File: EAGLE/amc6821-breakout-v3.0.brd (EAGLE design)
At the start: 45.7 x 45.8 mm, 68 parts, among them J1 QWIIC_RIGHT_ANGLE, J10 455-1750-1-ND, J2 QWIIC_RIGHT_ANGLE, J5 KK-254-4KK-254, J6 FAN No2, Q1 2N3904, Q2 2N7002, Q5 NDT3055L, U1 AMC6821-Q1QSOP-16N, U2 SN74LVC2G14DCKR, U3 SN74LVC2G14DCKR, U4 LD1117-33, U5 7805TV

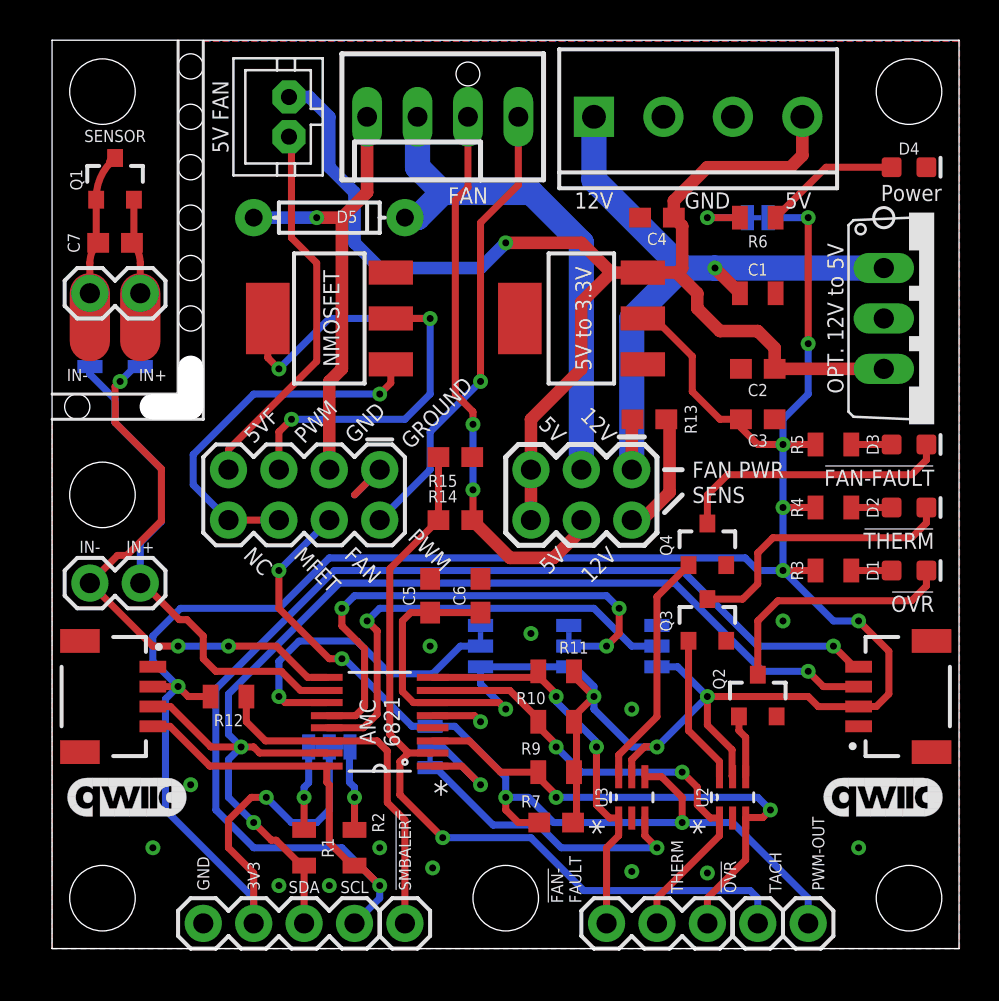
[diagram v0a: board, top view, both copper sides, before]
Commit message: v3 upload - split into 2 boards
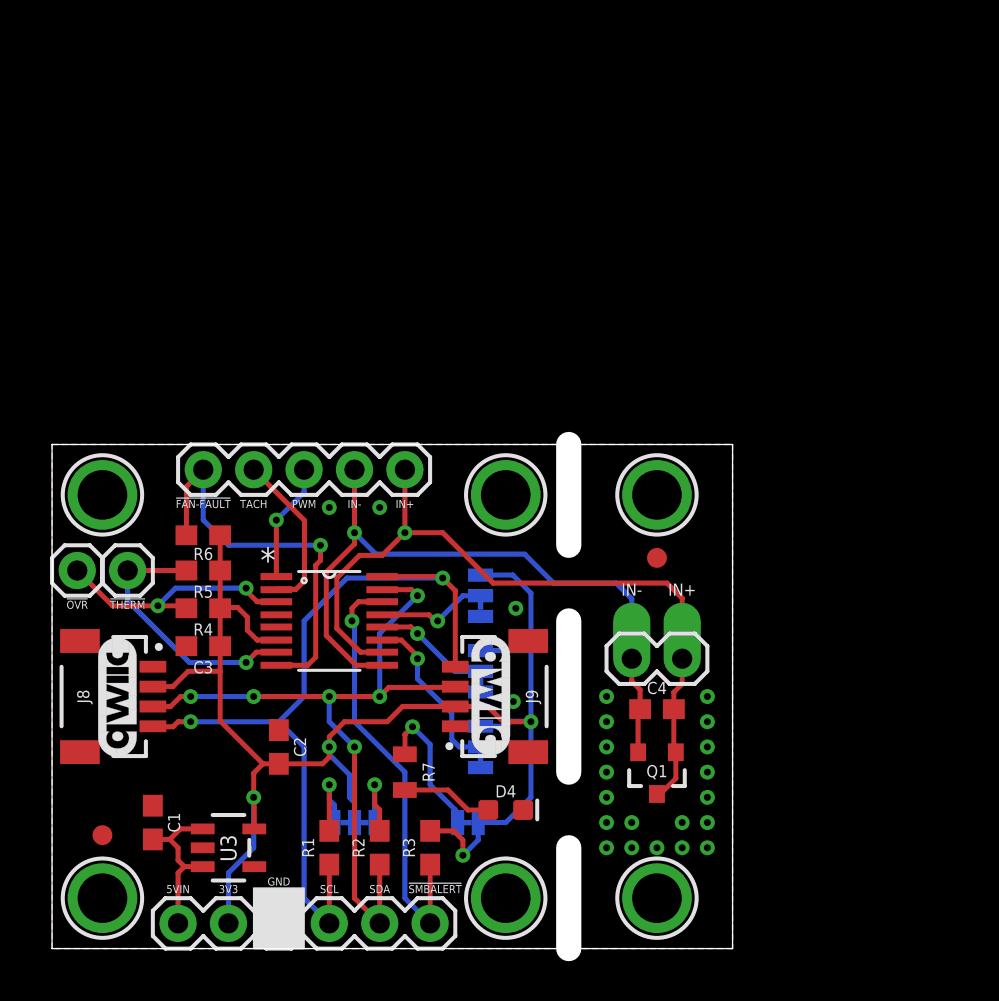
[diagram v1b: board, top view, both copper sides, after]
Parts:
- removed C5: 10uF, SparkFun-Capacitors:0603
- removed C6: 0.1uF, SparkFun-Capacitors:0603
- removed C7: 1nF, SparkFun-Capacitors:0603
- removed D1, D2, D3: RED, SparkFun-LED:LED-0603
- removed D5: 200mA/100V/1V, SparkFun-DiscreteSemi:DIODE-1N4148
- removed H1, H2, H3, H4, H5, H6: STAND-OFF, SparkFun-Hardware:STAND-OFF
- removed J1, J2: QWIIC_RIGHT_ANGLE, SparkFun-Connectors:JST04_1MM_RA
- removed J10: 455-1750-1-ND, SparkFun-Connectors:1X03
- removed J11, J12, J13: (no value), SparkFun-Connectors:1X01
- removed J14: (no value), SparkFun-Connectors:1X02
- removed JP4: JUMPER-SMT_3_1-NC_TRACE_SILK, SparkFun-Jumpers:SMT-JUMPER_3_1-NC_TRACE_SILK
- removed JP6, JP7: JUMPER-SMT_2_NC_TRACE_SILK, SparkFun-Jumpers:SMT-JUMPER_2_NC_TRACE_SILK
- removed JP8: (no value), SparkFun-Connectors:2X4
- removed JP9: (no value), SparkFun-Connectors:2X3-NS
- removed Q2: 2N7002, VinoRodrigues_Custom_Eagle:SOT23-3
- removed Q3, Q4: (no value), VinoRodrigues_Custom_Eagle:SOT23-3
- removed Q5: NDT3055L, VinoRodrigues_Custom_Eagle:SOT223
- removed R10, R11, R12, R9: 4.7K, SparkFun-Resistors:0805
- removed R13, R14: 10k, SparkFun-Resistors:0603
- removed R15: 4.7k, SparkFun-Resistors:0603
- removed U2: SN74LVC2G14DCKR, VinoRodrigues_Custom_Eagle:SOT65P210X110-6N
- removed U4: LD1117-33, SparkFun-IC-Power:SOT223
- removed U5: 7805TV, linear:TO220V
- added FID3, FID4: FIDUCIAL_1MM, microbuilder:FIDUCIAL_1MM
- added J7: (no value), VinoRodrigues_Custom_Eagle:1X02-LONG
- added J8: QWIIC_RIGHT_ANGLE, VinoRodrigues_Custom_Eagle:JST04_1MM_RA
- added U$10, U$4, U$5, U$7, U$8, U$9: MOUNTINGHOLE2.5, microbuilder:MOUNTINGHOLE_2.5_PLATED
- C1: value 0.33µF -> 10uF; device SparkFun-Capacitors:0805 -> SparkFun-Capacitors:0603
- C2: value 0.1uF -> 10uF
- C3: value 10uF -> 0.1uF
- C4: value 10uF -> 1nF
- J3: device SparkFun-Connectors:1X04 -> SparkFun-Connectors:1X05
- J4: device SparkFun-Connectors:SCREWTERMINAL-3.5MM-4 -> SparkFun-Connectors:1X06
- J5: value KK-254-4KK-254 -> (none); device VinoRodrigues_Custom_Eagle:MOLEX_47053-1000 -> SparkFun-Connectors:1X01
- J6: value FAN No2 -> (none); device VinoRodrigues_Custom_Eagle:JST-PH2 -> SparkFun-Connectors:1X01
- J9: value (none) -> QWIIC_RIGHT_ANGLE; device SparkFun-Connectors:1X02 -> VinoRodrigues_Custom_Eagle:JST04_1MM_RA
- R1, R2: value 4.7K -> 2.2k; device SparkFun-Resistors:0805 -> SparkFun-Resistors:0603
- R3, R4, R5, R6: value 1K -> 2.2k; device SparkFun-Resistors:0805 -> SparkFun-Resistors:0603
- R7: value 2.2k -> 1K; device SparkFun-Resistors:0603 -> SparkFun-Resistors:0805
- U3: value SN74LVC2G14DCKR -> AP2112K-3.3; device VinoRodrigues_Custom_Eagle:SOT65P210X110-6N -> microbuilder:SOT23-5
- moved J4 45.7 mm to (6.35, 1.27)
- moved C1 40.5 mm to (5.08, 6.35), turned to 90 degrees
- moved Q1 40.5 mm to (30.5, 8.89), turned to 180 degrees
- moved D4 38.2 mm to (22.9, 6.99)
- moved JP5 33.8 mm to (21.0, 6.35)
- moved R5 32.4 mm to (7.62, 19.1)
- moved R6 32.2 mm to (7.62, 20.8), turned to 0 degrees
- moved R4 32.2 mm to (7.62, 17.1), turned to 0 degrees
- moved LOGO1 31.3 mm to (12.7, 17.9), turned to 0 degrees
- moved C2 30.7 mm to (11.4, 10.2), turned to 90 degrees
- moved C3 30.2 mm to (7.62, 15.2), turned to 180 degrees
- moved J5 29.4 mm to (1.27, 19.1), turned to 0 degrees
- moved J9 27.4 mm to (20.3, 12.7), turned to 90 degrees
- moved U$1 27.3 mm to (8.26, 9.53), turned to 0 degrees
- moved J3 25.0 mm to (17.8, 24.1), turned to 180 degrees
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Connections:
- removed net !PWM-OUT: JP4.3, U3.3
- removed net 12V: C1.1, J4.1, JP9.1, R13.1, U5.1
- removed net FAN-FAULT: Q4.1, U3.6
- removed net FAN-GND: D5.A, J5.1:GND, JP8.3
- removed net GND-5V: J6.2, JP8.7
- removed net GND-PWM: JP8.5, Q5.D, Q5.D2
- removed net N$10: D3.C, Q4.3
- removed net N$11: D1.A, R3.1
- removed net N$14: D1.C, Q2.3
- removed net N$15: D2.C, Q3.3
- removed net N$16: D2.A, R4.1
- removed net N$17: J5.3:TACH, JP9.4, R14.2
- removed net N$18: JP9.2, R13.2
- removed net N$2: C7.2, J9.1, JP6.2, Q1.1, Q1.3
- removed net N$7: C7.1, J9.2, JP7.2, Q1.2
- removed net N$9: D3.A, R5.2
- removed net OVR: Q2.1, U2.4
- removed net PWM-FAN: J5.4:PWM, JP8.2
- removed net PWM-MF: JP8.6, JP8.8, Q5.G
- removed net PWM-OUT: J12.1, JP4.1, JP8.4, R7.1, U3.4
- removed net THERM: Q3.1, U2.6
- removed net VDD: D5.C, J5.2:+12VDC, JP9.3
- net !FAN-FAULT: now also J3.5, R6.1; no longer J10.1, R11.1, U3.1
- net !OVR: now also J5.1, R4.1; no longer J10.3, R9.1, U2.3
- net !SMBALERT: now also J4.6, R3.1; no longer J11.1, R12.1
- net !THERM: now also J6.1, R5.1; no longer J10.2, R10.1, U2.1
- net 3V3: now also C2.1, J4.2, J8.2, J9.2, R5.2, R6.2; no longer C5.1, C6.1, J1.2, J2.2, J3.2, R10.2, R11.2, R12.2, R5.1, R7.2, R9.2, U2.5, U4.2
- net 5V: now also C1.1, J4.1, U3.1, U3.3; no longer C2.1, C4.1, J4.4, J6.1, JP9.5, JP9.6, U4.3, U5.3
- net GND: now also J8.1, J8.NC1, J8.NC2, J9.1, J9.NC1, J9.NC2; no longer C4.2, C5.2, C6.2, J1.1, J2.1, J3.1, J4.2, JP8.1, Q2.2, Q3.2, Q4.2, Q5.S, R15.1, U2.2, U4.1, U5.2
- net IN+: now also C4.2, J3.1, J7.2, Q1.1, Q1.3; no longer J14.1, JP6.1
- net IN-: now also C4.1, J3.2, J7.1, Q1.2; no longer J14.2, JP7.1
- net N$12: now also R7.2; no longer R6.2
- net N$3: now also R2.1; no longer R1.1
- net N$4: now also R1.1; no longer R2.1
- net N$8: now also R7.1; no longer R6.1
- net PWM: now also J3.3; no longer JP4.2
- net SCL: now also J4.4, J8.4, J9.4, R1.2; no longer J1.4, J2.4, J3.4, R2.2
- net SDA: now also J4.5, J8.3, J9.3, R2.2; no longer J1.3, J2.3, J3.3, R1.2
- net TACH: now also J3.4; no longer J13.1, R14.1, R15.2
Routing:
- net 3V3: track 173.7 -> 77.4 mm, vias 12 -> 4
- net 5V: track 68.2 -> 8.32 mm, vias 1 -> 0
- net PWM-OUT: track 46.3 -> 0.00 mm, vias 4 -> 0
- net 12V: track 35.2 -> 0.00 mm, vias 1 -> 0
- net TACH: track 41.3 -> 8.26 mm, vias 1 -> 0
- net SCL: track 72.2 -> 41.9 mm
- net N$17: track 28.3 -> 0.00 mm, vias 2 -> 0
- net GND-PWM: track 27.5 -> 0.00 mm, vias 3 -> 0
- net VDD: track 26.2 -> 0.00 mm
- net PWM-FAN: track 23.2 -> 0.00 mm, vias 1 -> 0
- net FAN-GND: track 23.0 -> 0.00 mm, vias 1 -> 0
- net SDA: track 59.8 -> 38.9 mm, vias 3 -> 6
- net N$6: track 26.1 -> 5.89 mm, vias 3 -> 1
- net GND-5V: track 19.2 -> 0.00 mm
- net PWM-MF: track 19.0 -> 0.00 mm, vias 1 -> 0
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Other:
- board size 45.7 x 45.8 mm -> 34.3 x 25.4 mm
- board text added: "(c) 2012 Tecsmith by: Vino Rodrigues"
- board text added: "5VIN"
- board text added: "AMC6821 Breakout http://c1k.it/amc6 Qwiic / STEMMA QT"
- board text added: "AMC6821 Breakout http://c1k.it/amc6 Temperature Sensor"
- board text added: "Gnd"
- board text added: "Rev. 3.0"
- board text added: "Vdd"
- board text added: "Vdd A1 Gnd"
- board text added: "Vdd PWM-MODE Gnd"
- board text removed: "!FAN- FAULT"
- board text removed: "!FAULT"
- board text removed: "!SMBA"
- board text removed: "+"
- board text removed: "-"
- board text removed: "12V"
- board text removed: "3-Wire"
- board text removed: "4-Wire"
- board text removed: "5V"
- board text removed: "5V FAN"
- board text removed: "5V to 3.3V"
- board text removed: "5V-Fan"
- board text removed: "5VF"
- board text removed: "A1"
- board text removed: "AMC 6821"
- board text removed: "AMC6821 Breakout Board | Rel 2.3 (c) 2020 Vino Rodrigues"
- board text removed: "FAN"
- board text removed: "FAN PWR"
- board text removed: "FAN SENS"
- board text removed: "GND 3V3 SDA SCL"
- board text removed: "GROUND"
- board text removed: "MFET"
- board text removed: "NC"
- board text removed: "NMOSFET"
- board text removed: "OPT. 12V to 5V"
- board text removed: "Off"
- board text removed: "Opensource Hardware http://c1k.it/amc6"
- board text removed: "PWM-OUT"
- board text removed: "PWM/M"
- board text removed: "PWM\\!PWM"
- board text removed: "Power"
- board text removed: "SENS"
- board text removed: "SENSOR"
- board text removed: "TEMP. SENSOR"
- board text removed: "THERM"
- board text removed: "U2"
- board text removed: "U3"
- board text removed: "VDD"
- board text removed: "http://tecsmith.com.au"

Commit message: move C3 closer to the IC
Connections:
- net 3V3: now also C3.2; no longer C3.1
- net GND: now also C3.1; no longer C3.2
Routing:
- net 3V3: track 77.4 -> 74.2 mm
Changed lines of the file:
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@@
 <drawing>
 <settings>
-<setting alwaysvectorfont="yes"/>
+<setting alwaysvectorfont="no"/>
 <setting verticaltext="up"/>
 </settings>
@@
 <contactref element="J4" pad="2"/>
 <contactref element="U3" pad="5"/>
-<contactref element="C3" pad="1"/>
 <wire x1="10.1901" y1="6.03" x2="10.1901" y2="7.5899" width="0.254" layer="1"/>
 <wire x1="10.1901" y1="7.5899" x2="10.16" y2="7.62" width="0.254" layer="1"/>
@@
 <wire x1="8.47" y1="20.828" x2="8.47" y2="19.05" width="0.254" layer="1"/>
 <wire x1="8.47" y1="19.05" x2="8.47" y2="17.145" width="0.254" layer="1"/>
-<wire x1="8.47" y1="17.145" x2="8.47" y2="15.24" width="0.254" layer="1"/>
 <wire x1="9.8425" y1="16.03866875" x2="9.8425" y2="16.7005" width="0.254" layer="1"/>
 <wire x1="11.303" y1="15.5448" x2="10.33636875" y2="15.5448" width="0.254" layer="1"/>
@@
 <wire x1="8.47" y1="11.469" x2="8.47" y2="13.97" width="0.254" layer="1"/>
 <via x="24.13" y="11.43" extent="1-16" drill="0.35"/>
-<wire x1="8.47" y1="13.97" x2="8.47" y2="15.24" width="0.254" layer="1"/>
 <wire x1="24.13" y1="11.43" x2="24.13" y2="15.0114" width="0.254" layer="16"/>
 <wire x1="24.13" y1="15.0114" x2="24.13" y2="17.907" width="0.254" layer="16"/>
@@
 <wire x1="20.701" y1="5.461" x2="20.701" y2="4.699" width="0.254" layer="1"/>
 <wire x1="20.232" y1="5.93" x2="20.701" y2="5.461" width="0.254" layer="1"/>
+<contactref element="C3" pad="2"/>
+<wire x1="6.77" y1="15.24" x2="8.47" y2="17.145" width="0" layer="19" extent="1-1"/>
+<wire x1="5.08" y1="13.2" x2="6.77" y2="15.24" width="0" layer="19" extent="1-1"/>
 </signal>
 <signal name="GND">
@@
 <contactref element="J4" pad="3"/>
 <contactref element="U3" pad="2"/>
-<contactref element="C3" pad="2"/>
 <contactref element="J8" pad="NC2"/>
 <contactref element="J8" pad="NC1"/>
@@
 <via x="13.97" y="22.225" extent="1-16" drill="0.35"/>
 <via x="16.51" y="22.225" extent="1-16" drill="0.35"/>
+<contactref element="C3" pad="1"/>
+<wire x1="33.02" y1="11.43" x2="33.02" y2="12.7" width="0" layer="19" extent="1-1"/>
+<wire x1="33.02" y1="10.16" x2="33.02" y2="11.43" width="0" layer="19" extent="1-1"/>
+<wire x1="33.02" y1="8.89" x2="33.02" y2="10.16" width="0" layer="19" extent="1-1"/>
+<wire x1="33.02" y1="7.62" x2="33.02" y2="8.89" width="0" layer="19" extent="1-1"/>
+<wire x1="33.02" y1="6.35" x2="33.02" y2="7.62" width="0" layer="19" extent="1-1"/>
+<wire x1="33.02" y1="5.08" x2="33.02" y2="6.35" width="0" layer="19" extent="1-1"/>
+<wire x1="31.75" y1="5.08" x2="33.02" y2="5.08" width="0" layer="19" extent="1-1"/>
+<wire x1="30.48" y1="5.08" x2="31.75" y2="5.08" width="0" layer="19" extent="1-1"/>
+<wire x1="31.75" y1="6.35" x2="33.02" y2="6.35" width="0" layer="19" extent="1-1"/>
+<wire x1="29.21" y1="5.08" x2="30.48" y2="5.08" width="0" layer="19" extent="1-1"/>
+<wire x1="27.94" y1="5.08" x2="29.21" y2="5.08" width="0" layer="19" extent="1-1"/>
+<wire x1="27.94" y1="6.35" x2="27.94" y2="5.08" width="0" layer="19" extent="1-1"/>
+<wire x1="27.94" y1="7.62" x2="27.94" y2="6.35" width="0" layer="19" extent="1-1"/>
+<wire x1="27.94" y1="8.89" x2="27.94" y2="7.62" width="0" layer="19" extent="1-1"/>
+<wire x1="27.94" y1="10.16" x2="27.94" y2="8.89" width="0" layer="19" extent="1-1"/>
+<wire x1="27.94" y1="11.43" x2="27.94" y2="10.16" width="0" layer="19" extent="1-1"/>
+<wire x1="27.94" y1="12.7" x2="27.94" y2="11.43" width="0" layer="19" extent="1-1"/>
+<wire x1="29.21" y1="6.35" x2="29.21" y2="5.08" width="0" layer="19" extent="1-1"/>
+<wire x1="23.995" y1="9.9" x2="27.94" y2="10.16" width="0" layer="19" extent="1-1"/>
+<wire x1="21.59" y1="9.1186" x2="23.995" y2="9.9" width="0" layer="19" extent="1-16"/>
+<wire x1="20.32" y1="11.2" x2="21.59" y2="9.1186" width="0" layer="19" extent="1-16"/>
+<wire x1="21.59" y1="12.9286" x2="20.32" y2="11.2" width="0" layer="19" extent="1-16"/>
+<wire x1="23.241" y1="12.446" x2="21.59" y2="12.9286" width="0" layer="19" extent="16-16"/>
+<wire x1="23.737" y1="6.985" x2="23.995" y2="9.9" width="0" layer="19" extent="1-1"/>
+<wire x1="23.995" y1="15.5" x2="23.241" y2="12.446" width="0" layer="19" extent="1-1"/>
+<wire x1="23.368" y1="17.145" x2="23.995" y2="15.5" width="0" layer="19" extent="1-1"/>
+<wire x1="21.59" y1="16.7386" x2="23.368" y2="17.145" width="0" layer="19" extent="16-16"/>
+<wire x1="16.51" y1="22.225" x2="21.59" y2="16.7386" width="0" layer="19" extent="16-16"/>
+<wire x1="13.97" y1="22.225" x2="16.51" y2="22.225" width="0" layer="19" extent="1-1"/>
+<wire x1="11.303" y1="16.2052" x2="13.97" y2="22.225" width="0" layer="19" extent="1-1"/>
+<wire x1="8.47" y1="15.24" x2="11.303" y2="16.2052" width="0" layer="19" extent="1-1"/>
+<wire x1="5.08" y1="14.2" x2="8.47" y2="15.24" width="0" layer="19" extent="1-1"/>
+<wire x1="1.405" y1="15.5" x2="5.08" y2="14.2" width="0" layer="19" extent="1-1"/>
+<wire x1="11.43" y1="11.01" x2="8.47" y2="15.24" width="0" layer="19" extent="1-1"/>
+<wire x1="1.405" y1="9.9" x2="1.405" y2="15.5" width="0" layer="19" extent="1-1"/>
+<wire x1="5.08" y1="7.2" x2="1.405" y2="9.9" width="0" layer="19" extent="1-1"/>
+<wire x1="7.5899" y1="5.08" x2="5.08" y2="7.2" width="0" layer="19" extent="1-1"/>
+<wire x1="11.43" y1="1.27" x2="7.5899" y2="5.08" width="0" layer="19" extent="1-1"/>
 </signal>
 <signal name="N$3">

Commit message: minor rename, JP4
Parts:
- renumbered JP5 to JP4
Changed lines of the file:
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@@
 <attribute name="NAME" x="15.24" y="7.493" size="0.6096" layer="26" font="vector" ratio="20" rot="MR0" align="bottom-center"/>
 </element>
-<element name="JP5" library="SparkFun-Jumpers" package="SMT-JUMPER_2_NC_TRACE_SILK" package3d_urn="urn:adsk.eagle:package:39281/1" value="JUMPER-SMT_2_NC_TRACE_SILK" x="20.955" y="6.35" smashed="yes" rot="MR180"/>
+<element name="JP4" library="SparkFun-Jumpers" package="SMT-JUMPER_2_NC_TRACE_SILK" package3d_urn="urn:adsk.eagle:package:39281/1" value="JUMPER-SMT_2_NC_TRACE_SILK" x="20.955" y="6.35" smashed="yes" rot="MR180"/>
 <element name="LOGO1" library="SparkFun-Aesthetics" package="OSHW-LOGO-S" value="OSHW-LOGOS" x="12.7" y="17.907" smashed="yes" rot="MR0"/>
 <element name="LOGO2" library="SparkFun-Aesthetics" package="QWIIC_6MM" value="QWIIC_LOGO_6MM" x="3.302" y="12.7" smashed="yes" rot="R90"/>
@@
 <signal name="3V3">
 <contactref element="JP3" pad="2"/>
-<contactref element="JP5" pad="2"/>
+<contactref element="JP4" pad="2"/>
 <contactref element="C2" pad="1"/>
 <contactref element="JP0" pad="1"/>
@@
 </signal>
 <signal name="N$12">
-<contactref element="JP5" pad="1"/>
+<contactref element="JP4" pad="1"/>
 <contactref element="R7" pad="2"/>
 <via x="18.1638" y="11.176" extent="1-16" drill="0.35"/>

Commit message: minor edits
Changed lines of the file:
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@@
 <drawing>
 <settings>
-<setting alwaysvectorfont="no"/>
+<setting alwaysvectorfont="yes"/>
 <setting verticaltext="up"/>
 </settings>
@@
 <vertex x="12.7" y="0"/>
 </polygon>
+<hole x="26.035" y="6.985" drill="1"/>
 </plain>
 <attributes>

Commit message: updates
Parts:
- removed FID3, FID4: FIDUCIAL_1MM, microbuilder:FIDUCIAL_1MM
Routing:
- net 3V3: track 74.2 -> 87.4 mm, vias 4 -> 5
- net !FAN-FAULT: track 20.5 -> 17.0 mm
- net SDA: track 38.9 -> 36.7 mm
- net N$3: track 4.35 -> 5.36 mm
- net IN+: track 38.8 -> 38.0 mm, vias 1 -> 0
- net IN-: track 35.7 -> 35.0 mm
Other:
- outline, holes or cut-outs redrawn

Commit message: Update amc6821-breakout-v3.0.brd
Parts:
- moved J5 1.27 mm to (2.54, 19.1)
- moved J6 1.27 mm to (5.08, 19.1)
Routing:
- net 3V3: track 87.4 -> 88.4 mm
- net !OVR: track 12.7 -> 12.1 mm
- net !THERM: track 13.7 -> 14.3 mm
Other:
- outline, holes or cut-outs redrawn

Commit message: Update amc6821-breakout-v3.0.brd
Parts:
- moved Q1 1.27 mm to (30.5, 7.62)
- moved J5 1.27 mm to (1.27, 19.1)
- moved J6 1.27 mm to (3.81, 19.1)
- turned C3 to 0 degrees
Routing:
- net IN-: track 35.2 -> 37.6 mm
- net IN+: track 38.2 -> 40.1 mm
- net 3V3: track 88.4 -> 89.9 mm
- net !THERM: track 14.3 -> 15.5 mm
- net !OVR: track 12.1 -> 13.1 mm
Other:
- outline, holes or cut-outs redrawn

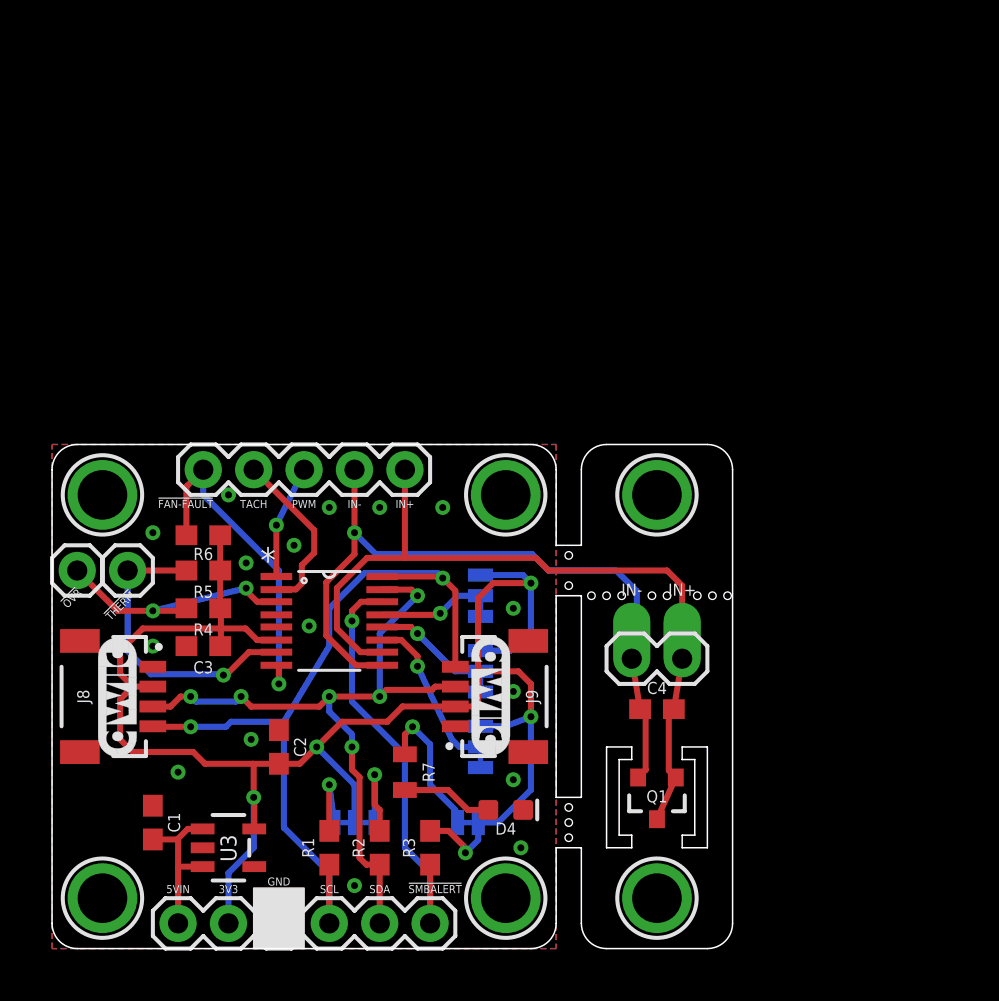
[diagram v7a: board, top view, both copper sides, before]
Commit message: rounded corners
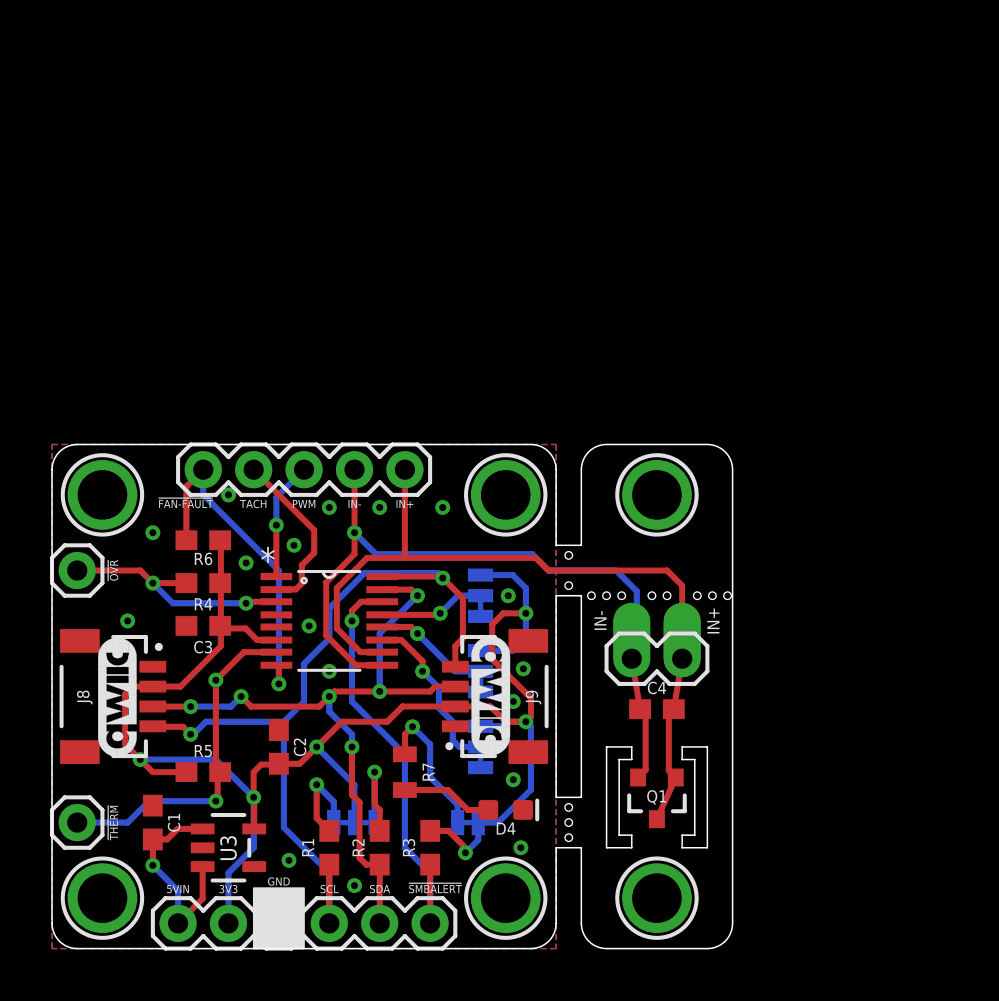
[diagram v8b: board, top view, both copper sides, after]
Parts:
- moved J6 13.0 mm to (1.27, 6.35)
- moved R5 10.2 mm to (7.62, 8.89), turned to 180 degrees
- moved U$1 2.05 mm to (10.2, 10.3)
- moved R4 1.27 mm to (7.62, 18.4)
- moved C3 1.02 mm to (7.62, 16.3)
- moved R6 0.25 mm to (7.62, 20.6)
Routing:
- net 3V3: track 89.9 -> 86.0 mm, vias 5 -> 6
- net 5V: track 8.24 -> 10.9 mm, vias 0 -> 1
- net !THERM: track 15.5 -> 17.4 mm, vias 1 -> 2
- net SCL: track 41.5 -> 42.4 mm
- net !OVR: track 13.1 -> 12.4 mm
- net N$4: track 4.31 -> 4.89 mm
